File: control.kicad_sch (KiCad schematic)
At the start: 5 parts, among them U13 74LS00, U17 74LS08, U4 74LS04, U5 74LS08

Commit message: Fix Oops...
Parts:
- removed unit 3 of U17
- removed U4: 74LS04, Package_DIP:DIP-14_W7.62mm, symbol 8bit-computer-rescue:74LS04-8bit-computer-rescue
- added unit 4 of U13
- C28: value .1uf -> 0.1uf
- U13: symbol 74xx:74LS00 -> 8bit-computer-rescue:74LS00-8bit-computer-rescue
- renumbered U5 to U17
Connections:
- net A12: now also U17.10; no longer U17.13
- net A13: now also U17.9; no longer U17.12
- net CS2Via2: now also U13.11
- net GND: now also U13.7 (GND), U13.7 (GND), U13.7 (GND), U13.7 (GND)
- net RAMOE: now also U17.8; no longer U17.11
- net ROMCS: now also U13.12
- net VCC: now also U13.14 (VCC), U13.14 (VCC), U13.14 (VCC), U13.14 (VCC)
- net at U17.6: now also U13.13

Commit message: Closer yet
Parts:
- removed unit 3 of U13
- removed U17: 74LS08, Package_DIP:DIP-14_W7.62mm, symbol 8bit-computer-rescue:74LS08-8bit-computer-rescue
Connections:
- net CS2Via2 is gone; now on net CS2: U13.11
- net A14: now also U13.13

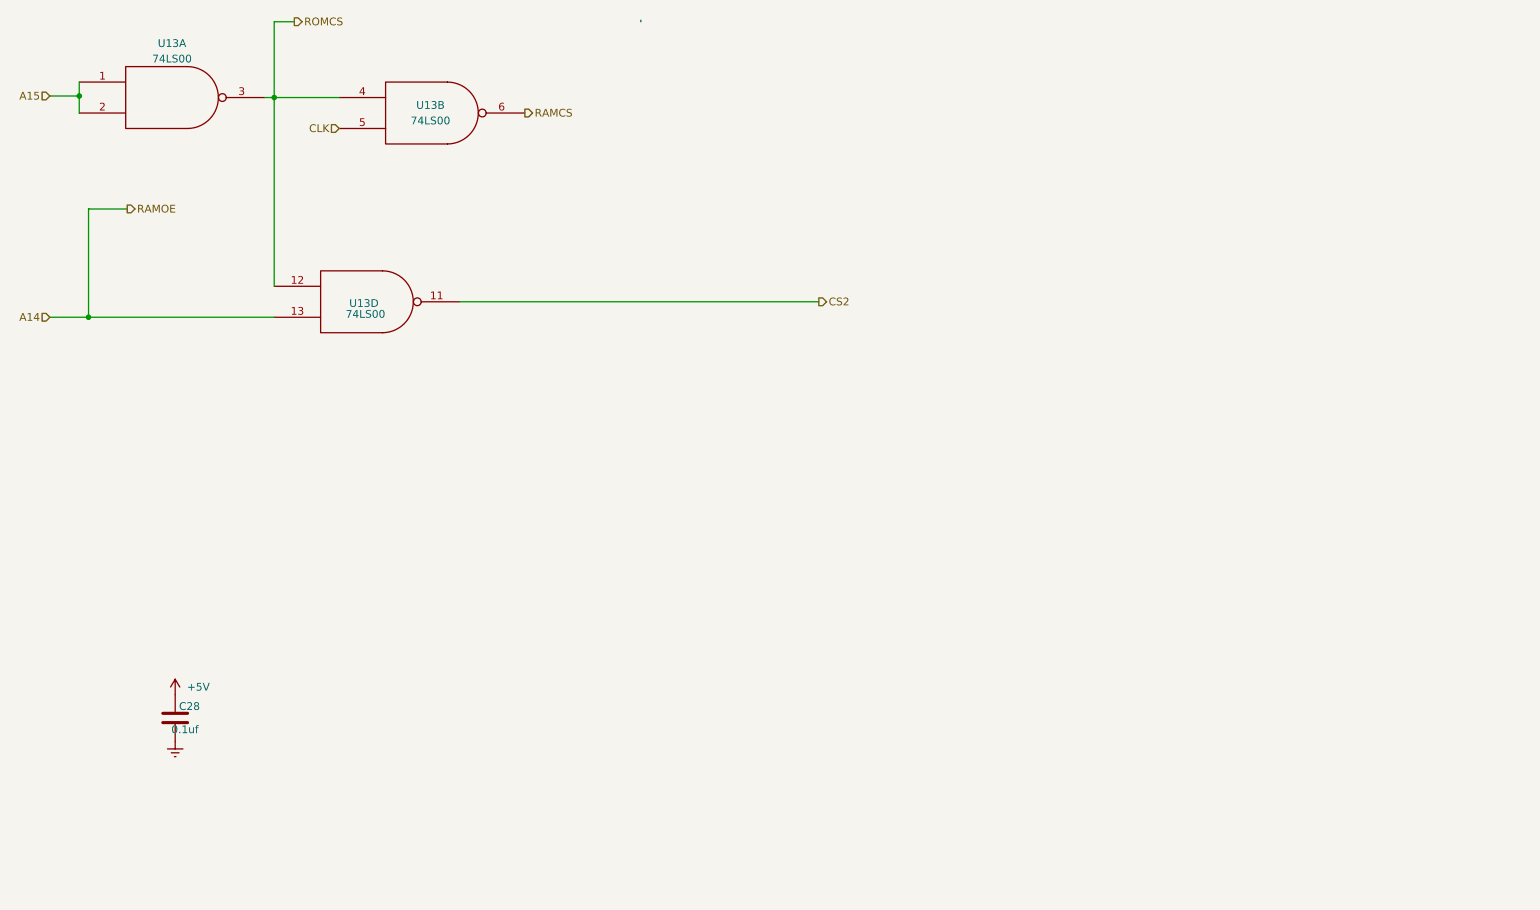
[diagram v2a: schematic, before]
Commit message: Fixed the addressing Still not fixed
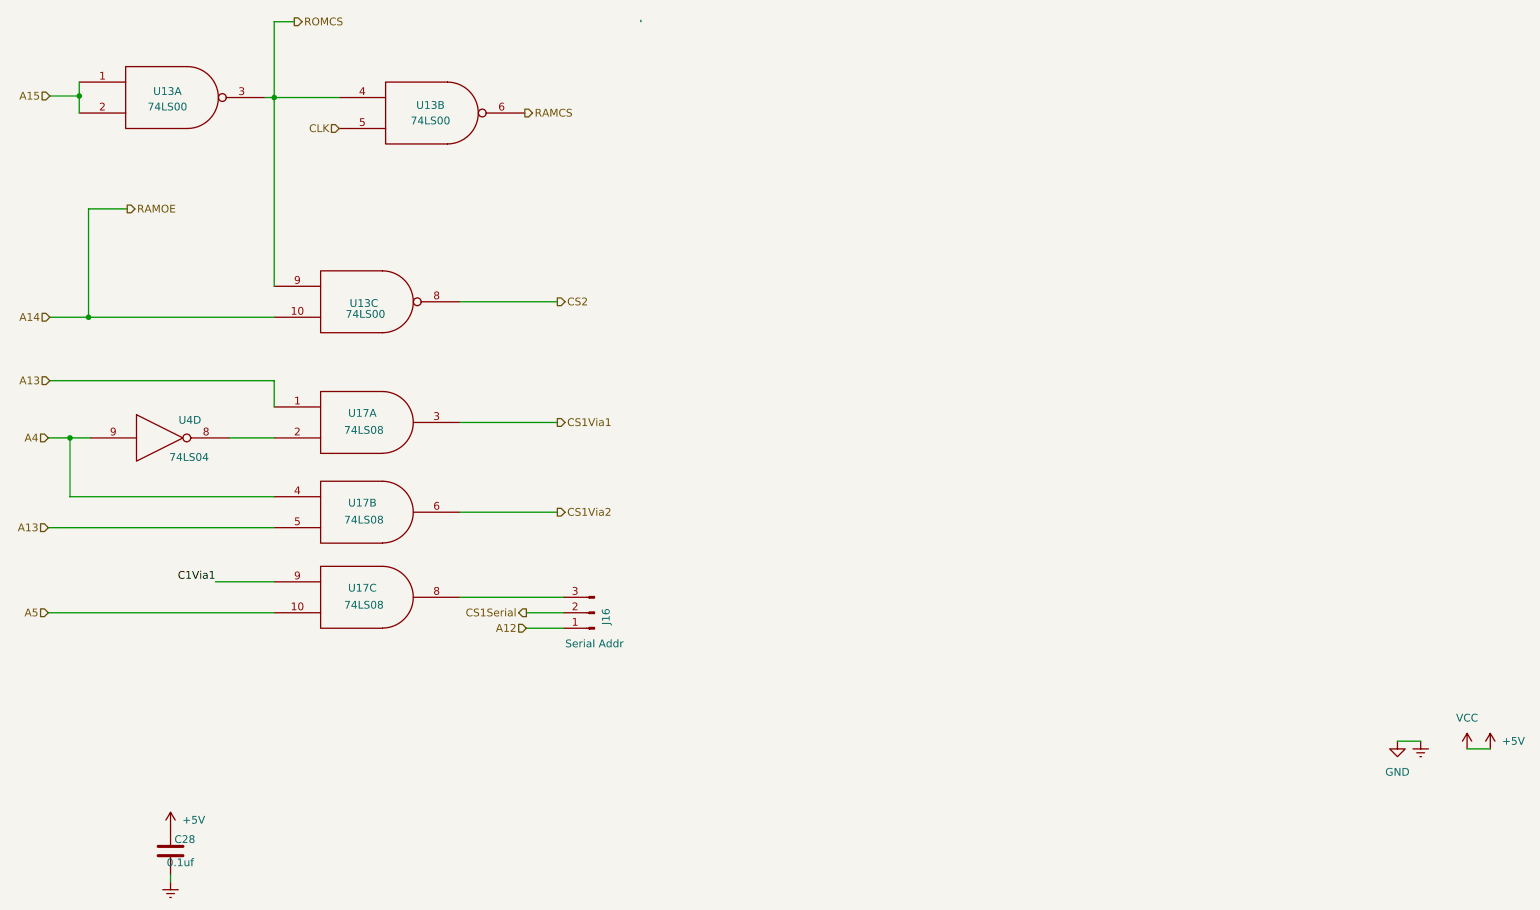
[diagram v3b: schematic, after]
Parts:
- added J16: Serial Addr, Connector_PinSocket_2.54mm:PinSocket_1x03_P2.54mm_Vertical, symbol Connector:Conn_01x03_Pin
- added U17: 74LS08, Package_DIP:DIP-14_W7.62mm, symbol 8bit-computer-rescue:74LS08-8bit-computer-rescue
- added U4: 74LS04, Package_DIP:DIP-14_W7.62mm, symbol 8bit-computer-rescue:74LS04-8bit-computer-rescue
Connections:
- net GND is gone; now on net Earth: U13.7 (GND), U13.7 (GND), U13.7 (GND)
- net VCC is gone; now on net +5V: U13.14 (VCC), U13.14 (VCC), U13.14 (VCC)
- net +5V: now also U17.14 (VCC), U17.14 (VCC), U17.14 (VCC), U4.14 (VCC)
- net A14: now also U13.10; no longer U13.13
- net CS2: now also U13.8; no longer U13.11
- net Earth: now also U17.7 (GND), U17.7 (GND), U17.7 (GND), U4.7 (GND)
- net ROMCS: now also U13.9; no longer U13.12
- new net: J16.3 (Pin_3), U17.8
- new net: U17.2, U4.8
- new net A12: J16.1 (Pin_1)
- new net A13: U17.1, U17.5
- new net A4: U17.4, U4.9
- new net A5: U17.10
- new net C1Via1: U17.9
- new net CS1Serial: J16.2 (Pin_2)
- new net CS1Via1: U17.3
- new net CS1Via2: U17.6
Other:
- moved on the sheet: C28
